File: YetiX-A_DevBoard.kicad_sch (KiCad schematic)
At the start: 57 parts, among them IC101 MCXA156VLH, J1 CONN HEADER VERT 22POS 2.54MM, J101 USB4105GFA120, J102 FTS-105-01-F-DV-P-TR, J2 CONN HEADER VERT 22POS 2.54MM, SW101 KMR421GULCLFS, SW102 KMR421GULCLFS, U1 M95256-DFMN6TP, U101 RCLAMP0854P.TCT, U102 XC6227C331PR-G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

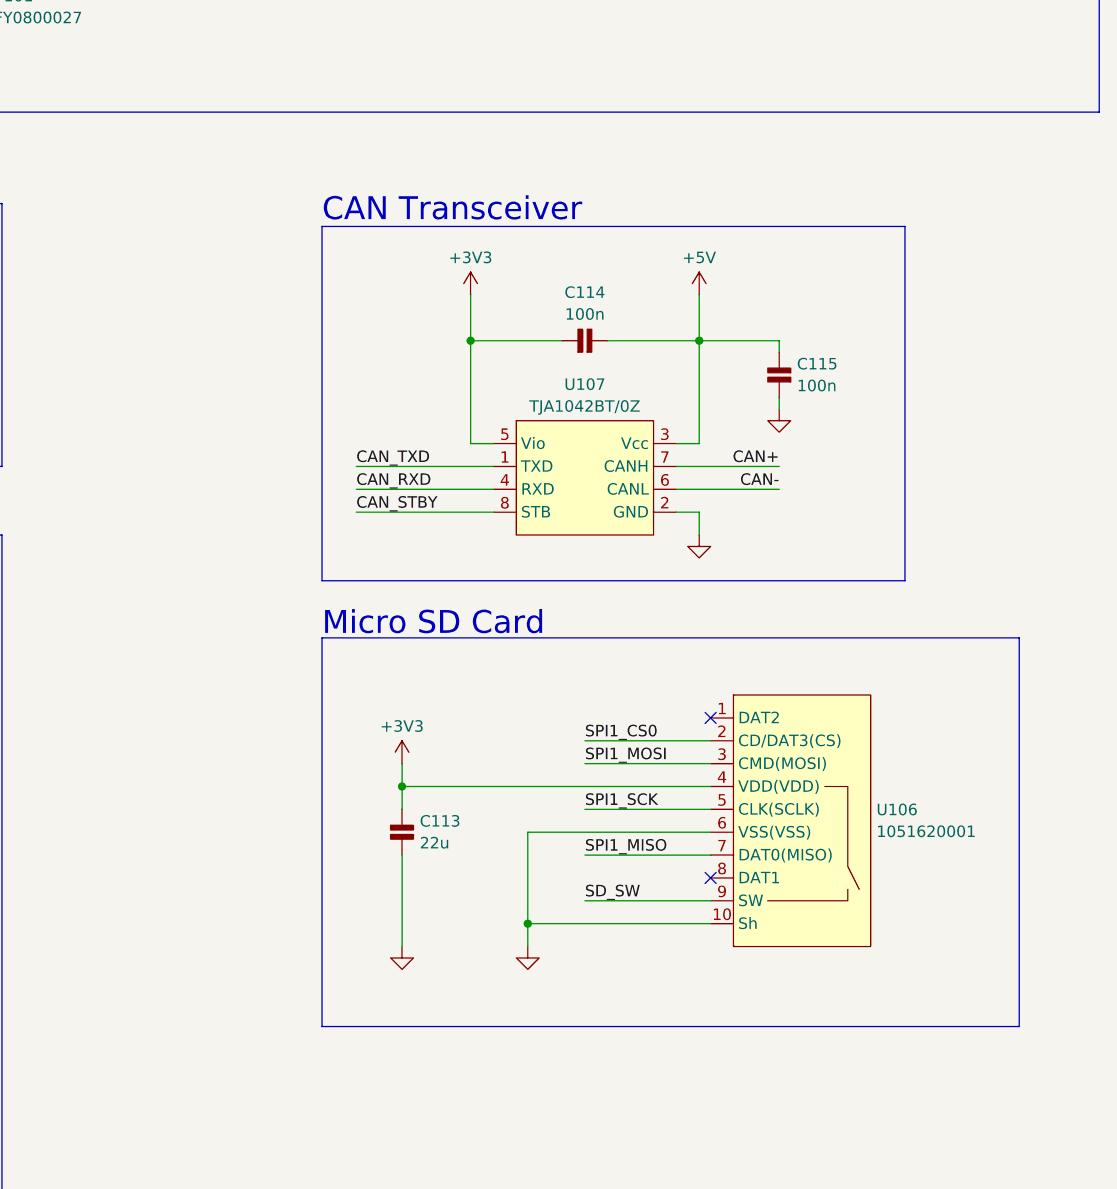
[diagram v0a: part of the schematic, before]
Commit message: Rev: 0.0.2
- Added filtering capacitors on CAN output.
- Added optional CAN termination
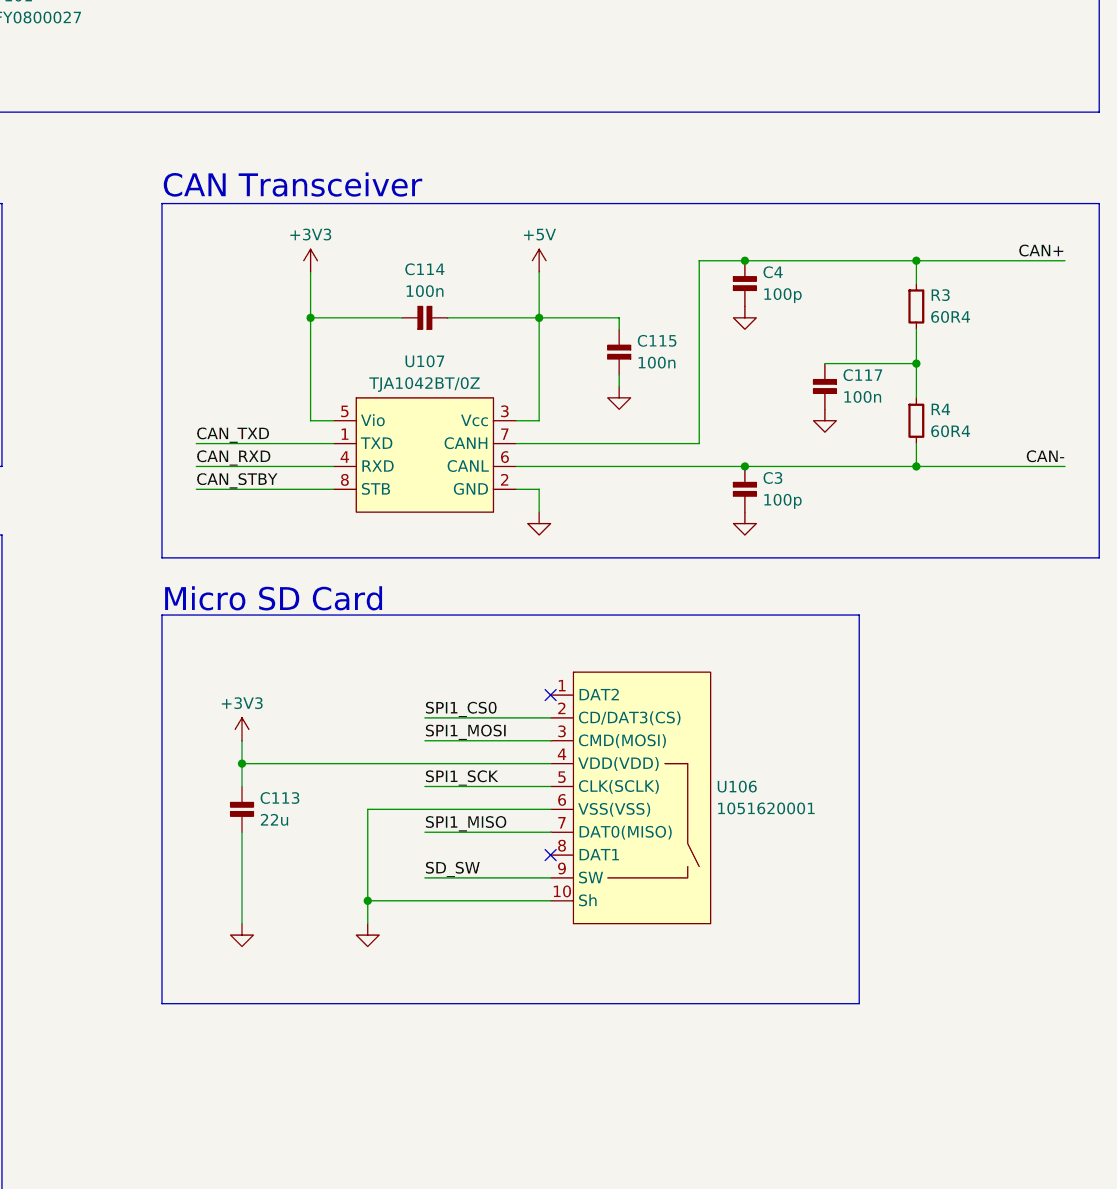
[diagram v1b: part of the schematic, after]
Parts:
- added C117: 100n, passive:C_0603, symbol db:capacitor/01.018.0025.0001
- added C3, C4: 100p, passive:C_0603, symbol db:capacitor/01.018.0025.0005
- added R3, R4: 60R4, passive:R_0805, symbol db:resistor/00.018.0009.0021
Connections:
- net CAN+: now also C4.1, R3.1
- net CAN-: now also C3.1, R4.2
- net GND: now also C117.1, C3.2, C4.2
- new net: C117.2, R3.2, R4.1
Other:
- moved on the sheet: C113, C114, C115, U106, U107
